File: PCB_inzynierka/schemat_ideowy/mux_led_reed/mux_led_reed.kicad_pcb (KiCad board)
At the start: 4 copper layers, 70 parts, among them J1 Conn_01x01_Pin, J2 Conn_01x03_Pin, J3 Conn_01x01_Pin, J4 Conn_01x03_Pin, SW1 SW_Reed, SW10 SW_Reed, SW11 SW_Reed, SW12 SW_Reed, SW13 SW_Reed, SW14 SW_Reed, SW15 SW_Reed, SW16 SW_Reed, SW2 SW_Reed, SW3 SW_Reed, SW4 SW_Reed, SW5 SW_Reed, SW6 SW_Reed, SW7 SW_Reed, SW8 SW_Reed, SW9 SW_Reed, U1 74HC4051D_653, U2 74HC4051D_653

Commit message: first version of 4x4 pcb for chessboard
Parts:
- added J5: Conn_01x04_Pin, Connector_PinHeader_2.54mm:PinHeader_1x04_P2.54mm_Horizontal, F.Cu at (155.6, 146.0)
- added J6: Conn_01x04_Pin, Connector_PinHeader_2.54mm:PinHeader_1x04_P2.54mm_Horizontal, F.Cu at (180.5, 146.0)
- added J7: Conn_01x04_Pin, Connector_PinSocket_2.54mm:PinSocket_1x04_P2.54mm_Horizontal, F.Cu at (180.5, 51.5)
- added J8: Conn_01x04_Pin, Connector_PinSocket_2.54mm:PinSocket_1x04_P2.54mm_Horizontal, F.Cu at (155.6, 51.5)
- added JP1: SolderJumper_2_Open, Jumper:SolderJumper-2_P1.3mm_Open_Pad1.0x1.5mm, F.Cu at (104.2, 148.0)
- added JP2: SolderJumper_2_Open, Jumper:SolderJumper-2_P1.3mm_Open_Pad1.0x1.5mm, F.Cu at (194.0, 125.0)
- added JP3: SolderJumper_2_Open, Jumper:SolderJumper-2_P1.3mm_Open_Pad1.0x1.5mm, F.Cu at (104.5, 100.0)
- added JP4: SolderJumper_2_Open, Jumper:SolderJumper-2_P1.3mm_Open_Pad1.0x1.5mm, F.Cu at (194.0, 75.0)
- added JP5: SolderJumper_2_Open, Jumper:SolderJumper-2_P1.3mm_Open_Pad1.0x1.5mm, F.Cu at (103.5, 51.6)
- added TP11: VDD_OUT, TestPoint:TestPoint_Pad_4.0x4.0mm, F.Cu at (123.5, 52.5)
- added TP12: GND_OUT, TestPoint:TestPoint_Pad_4.0x4.0mm, F.Cu at (128.5, 52.5)
- C17, C18, J2, J4, U1, U2: moved to B.Cu
- J1, J3: footprint Connector_PinHeader_2.00mm:PinHeader_1x01_P2.00mm_Vertical -> Connector_PinHeader_2.54mm:PinHeader_1x01_P2.54mm_Vertical; moved to B.Cu
- TP1, TP2, TP3, TP4, TP5, TP6, TP7, TP8: footprint TestPoint:TestPoint_Pad_4.0x4.0mm -> TestPoint:TestPoint_Pad_3.0x3.0mm
- TP10: value TestPoint -> GND_IN
- TP9: value TestPoint -> VDD_IN
- moved C1 256.9 mm to (118.5, 142.0), turned to 180 degrees
- moved C8 247.0 mm to (106.5, 107.5)
- moved TP8 243.9 mm to (102.0, 62.5)
- moved R1 239.2 mm to (106.5, 137.5), turned to 90 degrees
- moved C2 237.6 mm to (143.5, 142.0), turned to 180 degrees
- moved SW4 237.1 mm to (187.5, 137.5), turned to -90 degrees
- moved TP5 234.8 mm to (102.0, 87.5)
- moved R3 232.4 mm to (106.5, 87.5), turned to 90 degrees
- moved TP4 229.6 mm to (102.0, 112.5)
- moved TP1 229.4 mm to (102.0, 137.5)
- moved SW13 228.6 mm to (187.5, 62.5), turned to 90 degrees
- moved SW5 227.7 mm to (187.5, 112.5), turned to 90 degrees
- moved C9 226.5 mm to (118.5, 92.0), turned to 180 degrees
- moved C18 224.1 mm to (155.0, 131.5), turned to -90 degrees
- moved C16 224.1 mm to (106.5, 58.0)
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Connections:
- C10 pad 1: +5V -> GND
- C10 pad 2: GND -> +5V
- C17 pad 1: GND -> +5V
- C17 pad 2: +5V -> GND
- C18 pad 1: GND -> +5V
- C18 pad 2: +5V -> GND
- C9 pad 1: +5V -> GND
- C9 pad 2: GND -> +5V
- D12 pad 2: /DOUT_1 -> /DOUT_2
- D13 pad 2: /DOUT_3 -> Net-(D13-DOUT)
- D14 pad 2: Net-(D13-DIN) -> Net-(D14-DOUT)
- D14 pad 4: Net-(D14-DIN) -> Net-(D13-DOUT)
- D15 pad 2: Net-(D14-DIN) -> Net-(D15-DOUT)
- D15 pad 4: Net-(D15-DIN) -> Net-(D14-DOUT)
- D16 pad 2: Net-(D15-DIN) -> /DOUT_3
- D16 pad 4: Net-(D16-DIN) -> Net-(D15-DOUT)
- D8 pad 2: /DOUT_2 -> /DOUT_1
- R2 pad 2: Net-(D9-DIN) -> Net-(D5-DIN)
- R3 pad 1: /DIN_3 -> /DIN_2
- R3 pad 2: Net-(D16-DIN) -> Net-(D9-DIN)
- R4 pad 1: /DIN_2 -> /DIN_3
- R4 pad 2: Net-(D5-DIN) -> Net-(D13-DIN)
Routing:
- net +5V: track 0.00 -> 188.4 mm, vias 0 -> 36
- net GND: track 0.00 -> 103.0 mm, vias 0 -> 38
- net /Y04: track 0.00 -> 59.7 mm, vias 0 -> 2
- net /Y14: track 0.00 -> 58.3 mm, vias 0 -> 2
- net Net-(J1-Pin_1): track 0.00 -> 48.4 mm, vias 0 -> 2
- net /Y00: track 0.00 -> 48.1 mm
- net Net-(J3-Pin_1): track 0.00 -> 46.2 mm, vias 0 -> 2
- net /Y10: track 0.00 -> 45.5 mm
- net /Y07: track 0.00 -> 39.1 mm
- net /Y17: track 0.00 -> 39.1 mm
- net /Y13: track 0.00 -> 37.5 mm
- net /Y03: track 0.00 -> 37.5 mm
- net Net-(J2-Pin_3): track 0.00 -> 24.9 mm
- net Net-(J2-Pin_2): track 0.00 -> 24.2 mm
- net Net-(J4-Pin_1): track 0.00 -> 24.0 mm
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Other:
- board outline added: 100 x 100 mm
- board text added: "+5V"
- board text added: "+5V VDD"
- board text added: "DIN"
- board text added: "DOUT"
- board text added: "GND"
- board text added: "M_OUT"
- board text added: "S0"
- board text added: "S1"
- board text added: "S2"

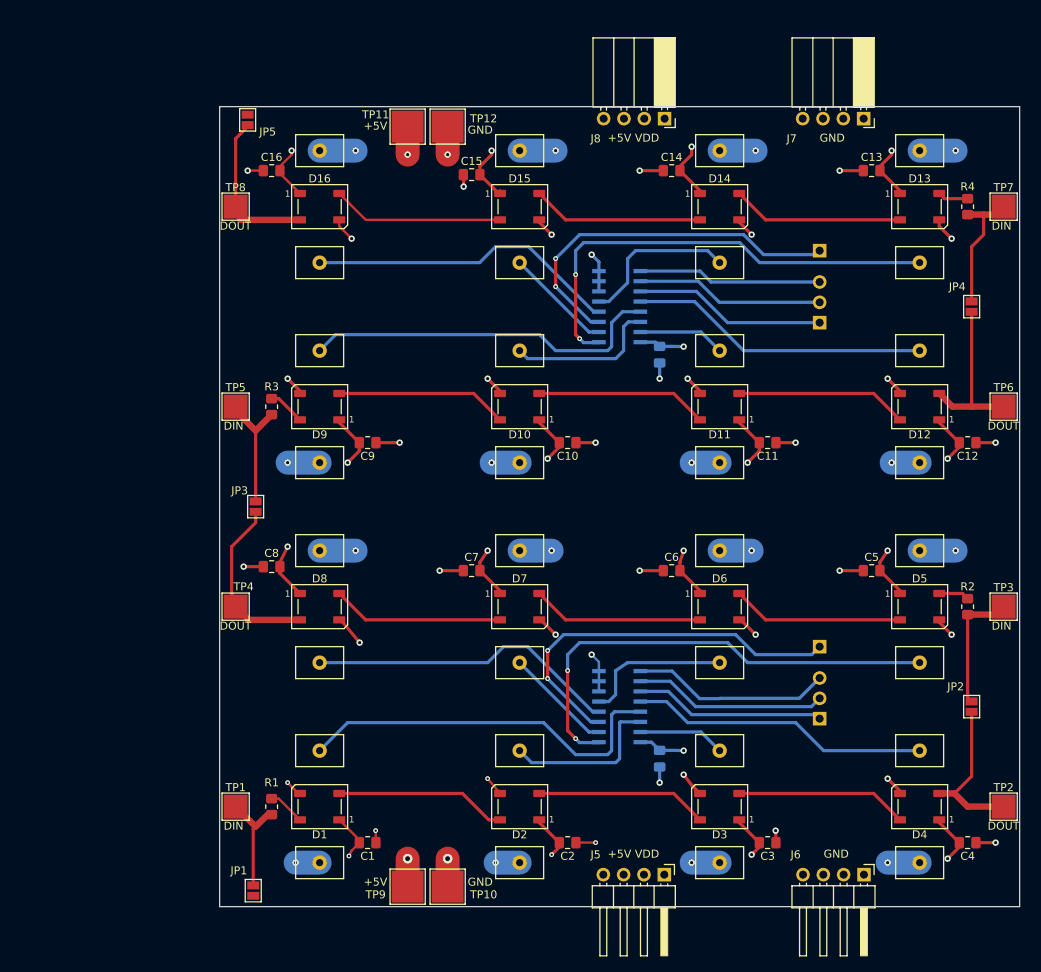
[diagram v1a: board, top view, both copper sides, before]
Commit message: plytka 4x4 zawierajaca mux, reed switche i ledy argb v1.0
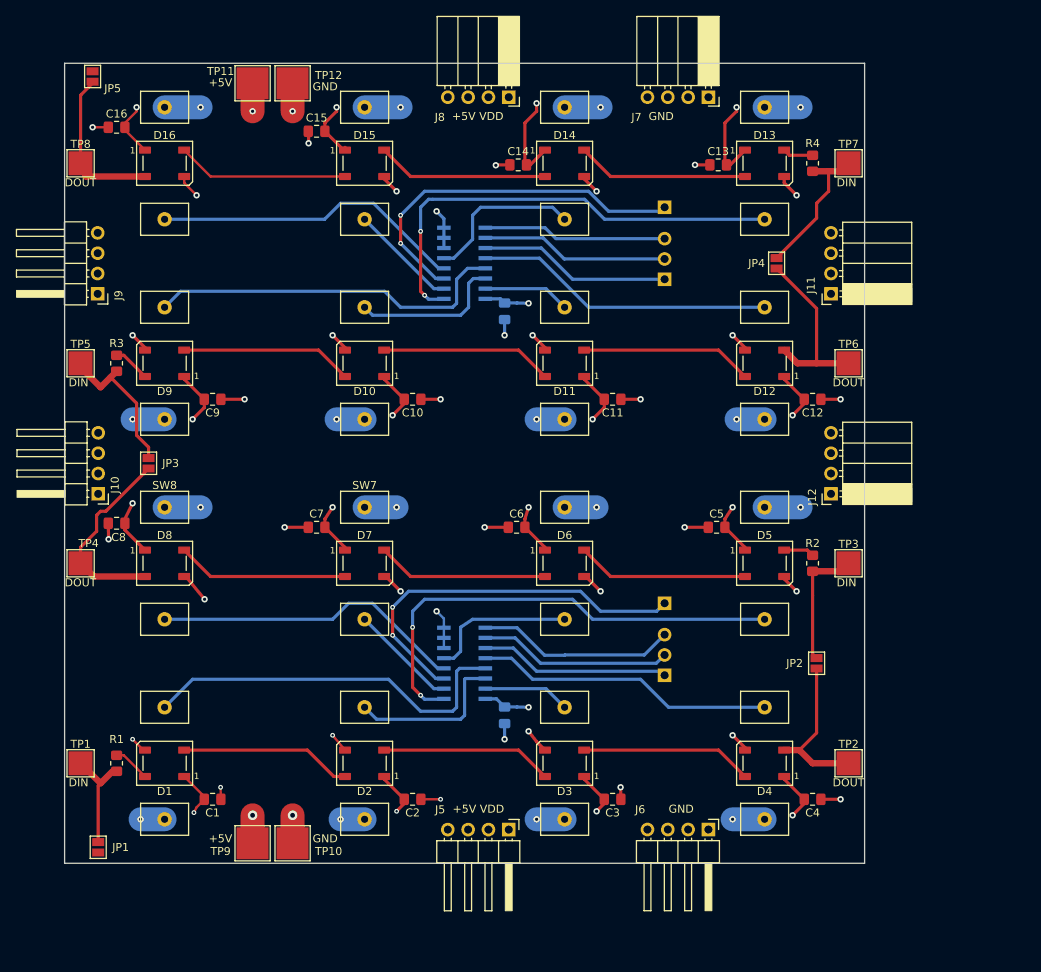
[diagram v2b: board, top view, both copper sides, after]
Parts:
- added J10: Conn_01x04_Pin, Connector_PinHeader_2.54mm:PinHeader_1x04_P2.54mm_Horizontal, F.Cu at (84.8, 98.4)
- added J11: Conn_01x04_Pin, Connector_PinSocket_2.54mm:PinSocket_1x04_P2.54mm_Horizontal, F.Cu at (176.4, 73.4)
- added J12: Conn_01x04_Pin, Connector_PinSocket_2.54mm:PinSocket_1x04_P2.54mm_Horizontal, F.Cu at (176.4, 98.4)
- added J9: Conn_01x04_Pin, Connector_PinHeader_2.54mm:PinHeader_1x04_P2.54mm_Horizontal, F.Cu at (84.8, 73.4)
- moved JP4 25.0 mm to (169.6, 69.6)
- moved J6 20.2 mm to (161.1, 140.4)
- moved J5 20.2 mm to (136.1, 140.4)
- moved JP5 20.1 mm to (84.1, 46.2)
- moved C10 20.1 mm to (124.1, 86.6)
- moved C11 20.1 mm to (149.1, 86.6)
- moved C12 20.1 mm to (174.1, 86.6)
- moved C15 20.1 mm to (112.1, 53.1)
- moved C16 20.1 mm to (87.1, 52.6)
- moved C17 20.1 mm to (135.6, 75.6)
- moved C18 20.1 mm to (135.6, 126.1)
- moved C5 20.1 mm to (162.1, 102.6)
- moved C6 20.1 mm to (137.1, 102.6)
- moved C7 20.1 mm to (112.1, 102.6)
- moved C8 20.1 mm to (87.1, 102.1)
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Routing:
- net +5V: track 188.4 -> 196.3 mm
- net /DOUT_1: track 23.0 -> 26.5 mm
- net /DIN_2: track 15.7 -> 18.9 mm
- net GND: track 103.0 -> 100.3 mm
- net /DIN_3: track 16.4 -> 18.5 mm
- net /DOUT_2: track 20.6 -> 22.7 mm

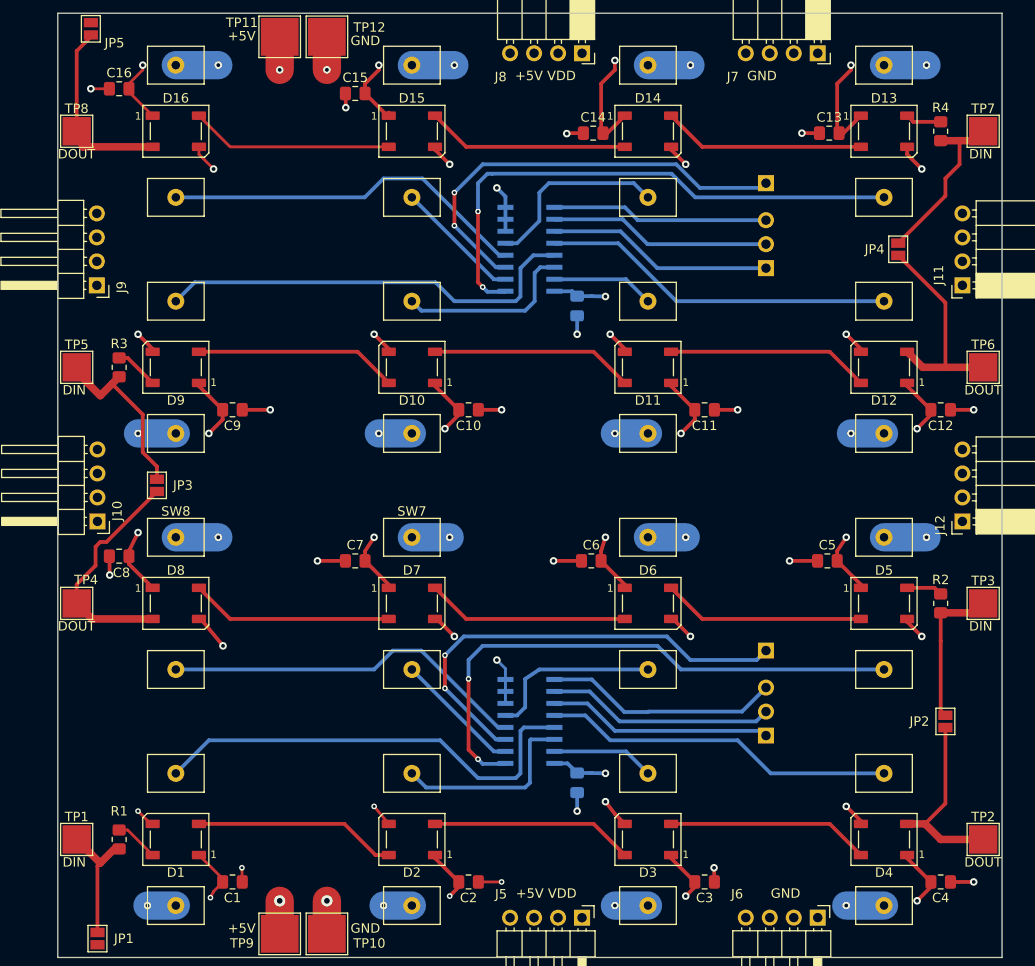
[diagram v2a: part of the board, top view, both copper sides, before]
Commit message: obie plytki pcb przygotowane, schematy ideowe opisane
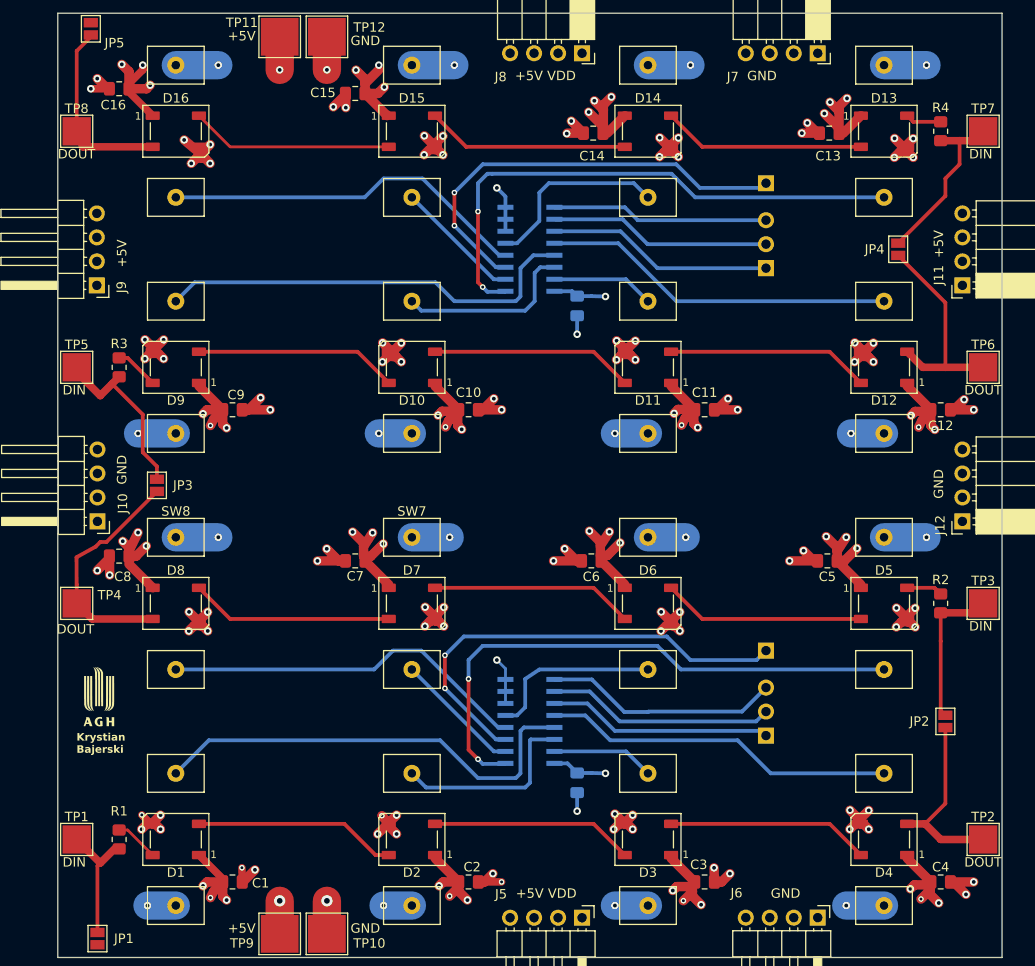
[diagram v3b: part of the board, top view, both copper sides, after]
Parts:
- added G***: LOGO, LOGO, F.Cu at (85.0, 117.0)
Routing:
- net GND: track 100.3 -> 216.9 mm, vias 38 -> 102
- net +5V: track 196.3 -> 293.0 mm, vias 36 -> 68
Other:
- board text added: "Krystian Bajerski"

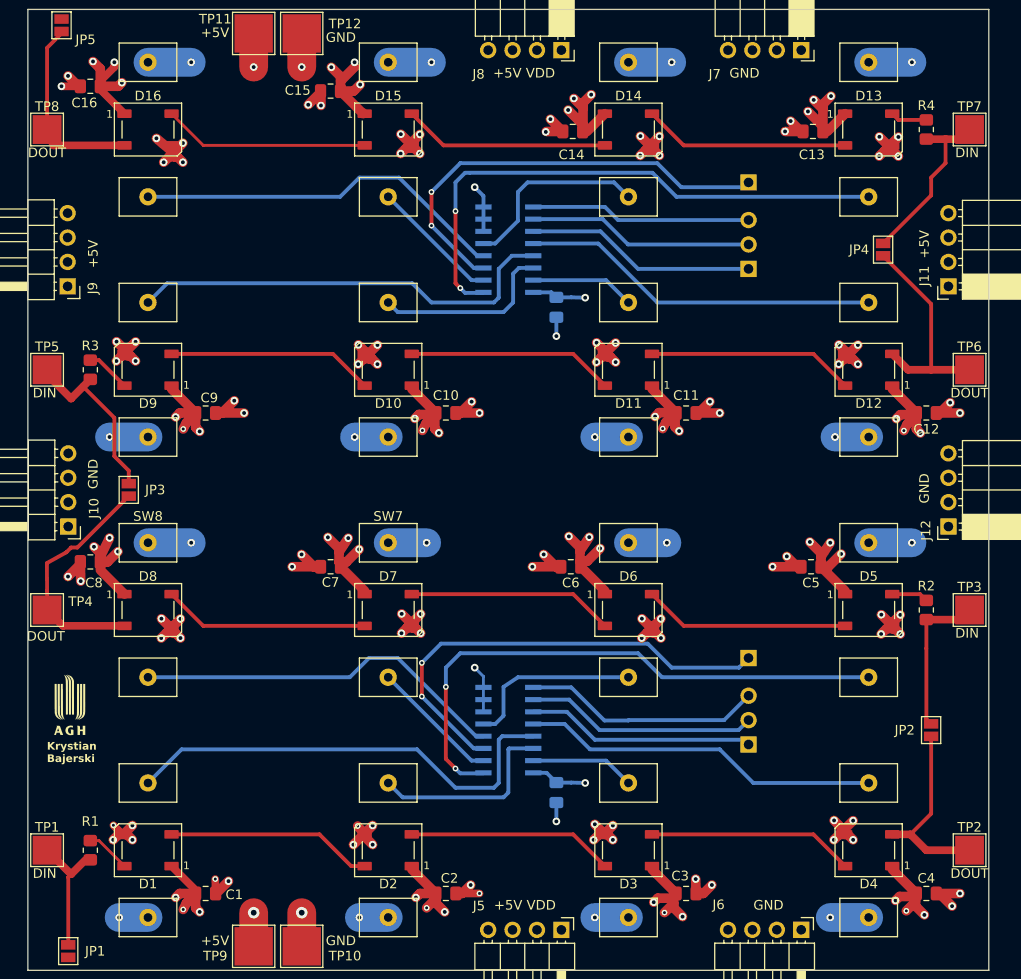
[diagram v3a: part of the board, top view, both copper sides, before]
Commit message: pcb v1.0, przygotowane pliki do fabryki pcb, zamowienie zlozone, poprawa przelotek
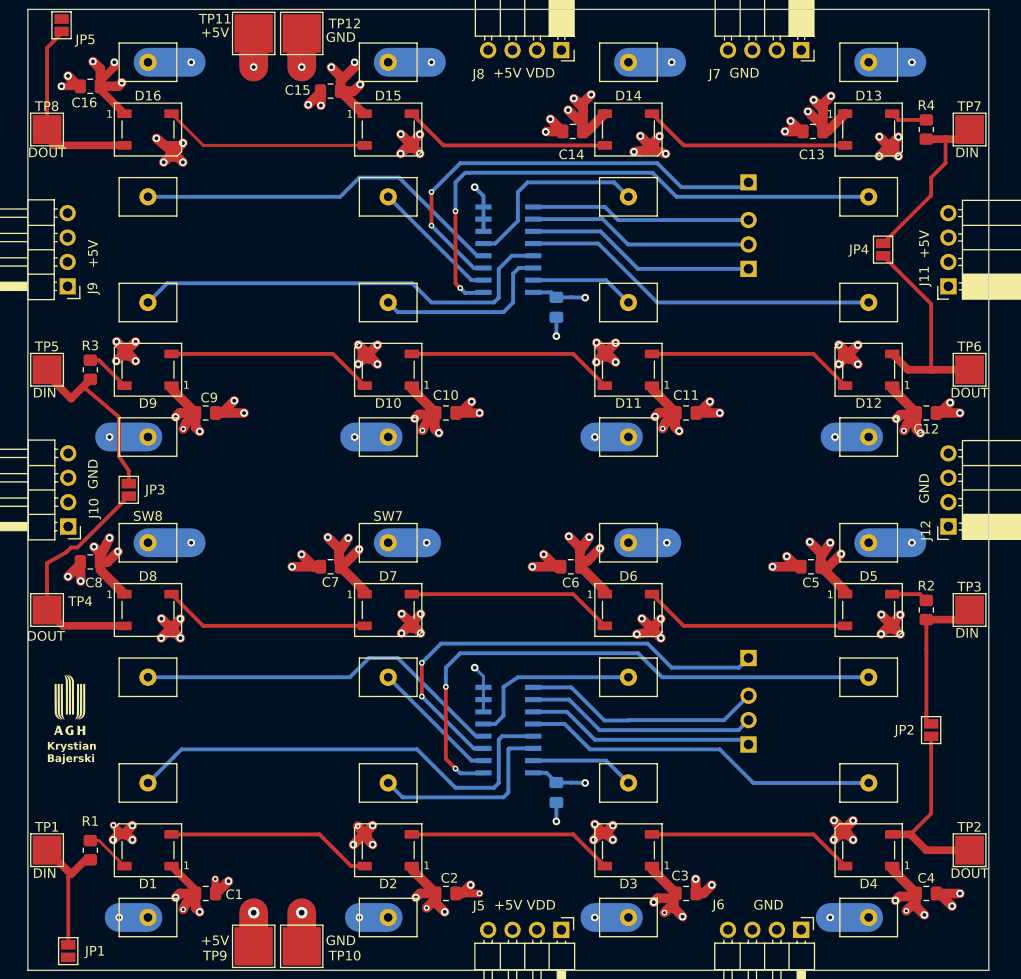
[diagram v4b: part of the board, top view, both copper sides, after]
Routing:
- net GND: track 216.9 -> 218.0 mm
